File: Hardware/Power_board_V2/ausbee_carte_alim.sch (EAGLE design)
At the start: 22 parts, among them K1 G5LE

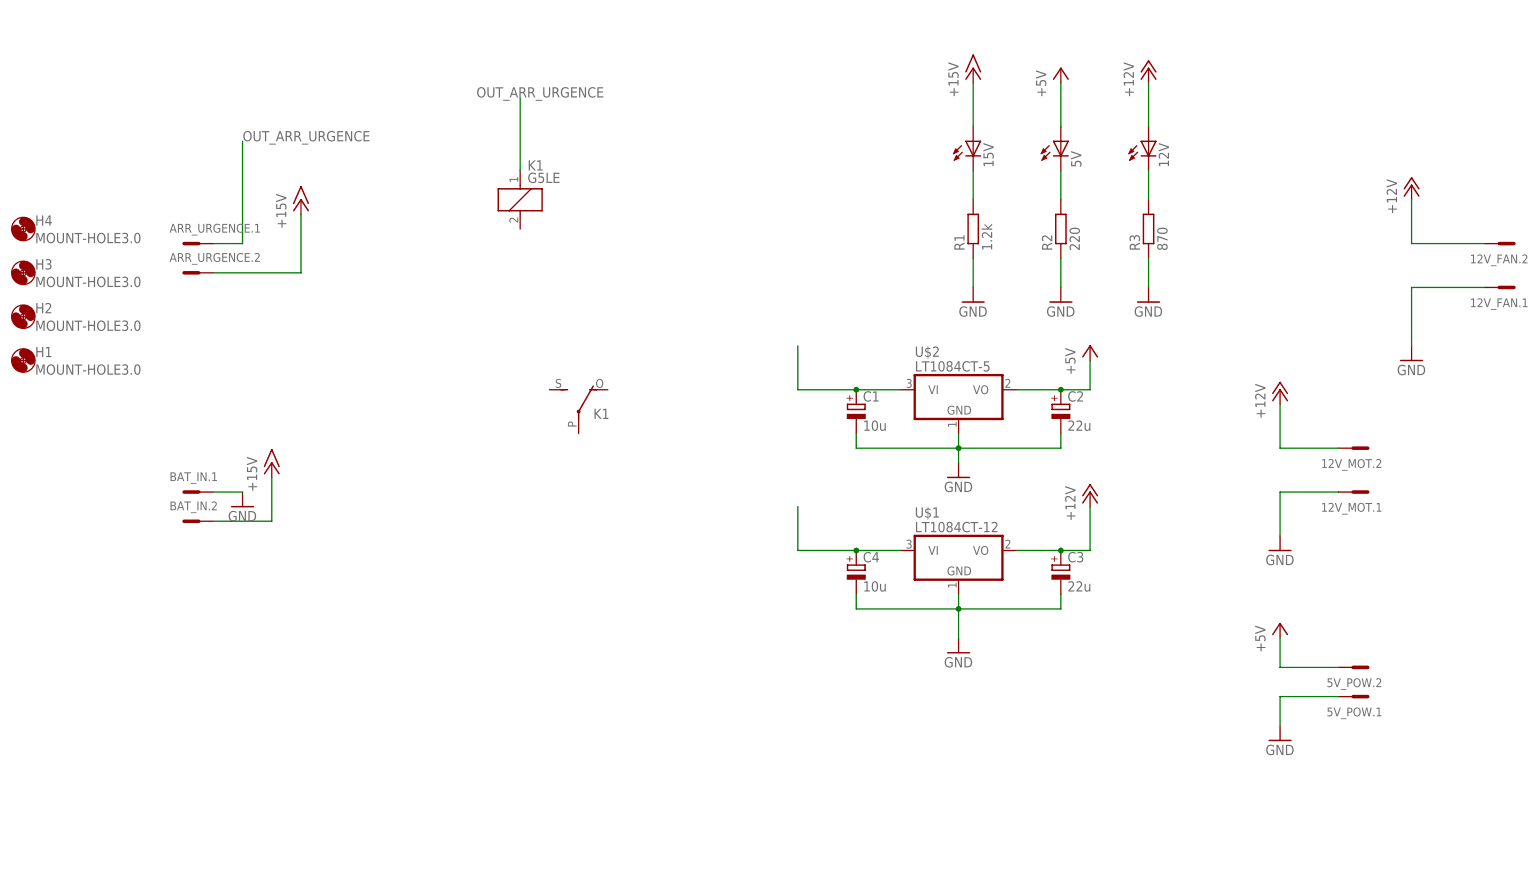
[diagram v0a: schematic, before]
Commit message: Power board V2, adaptator GPIO
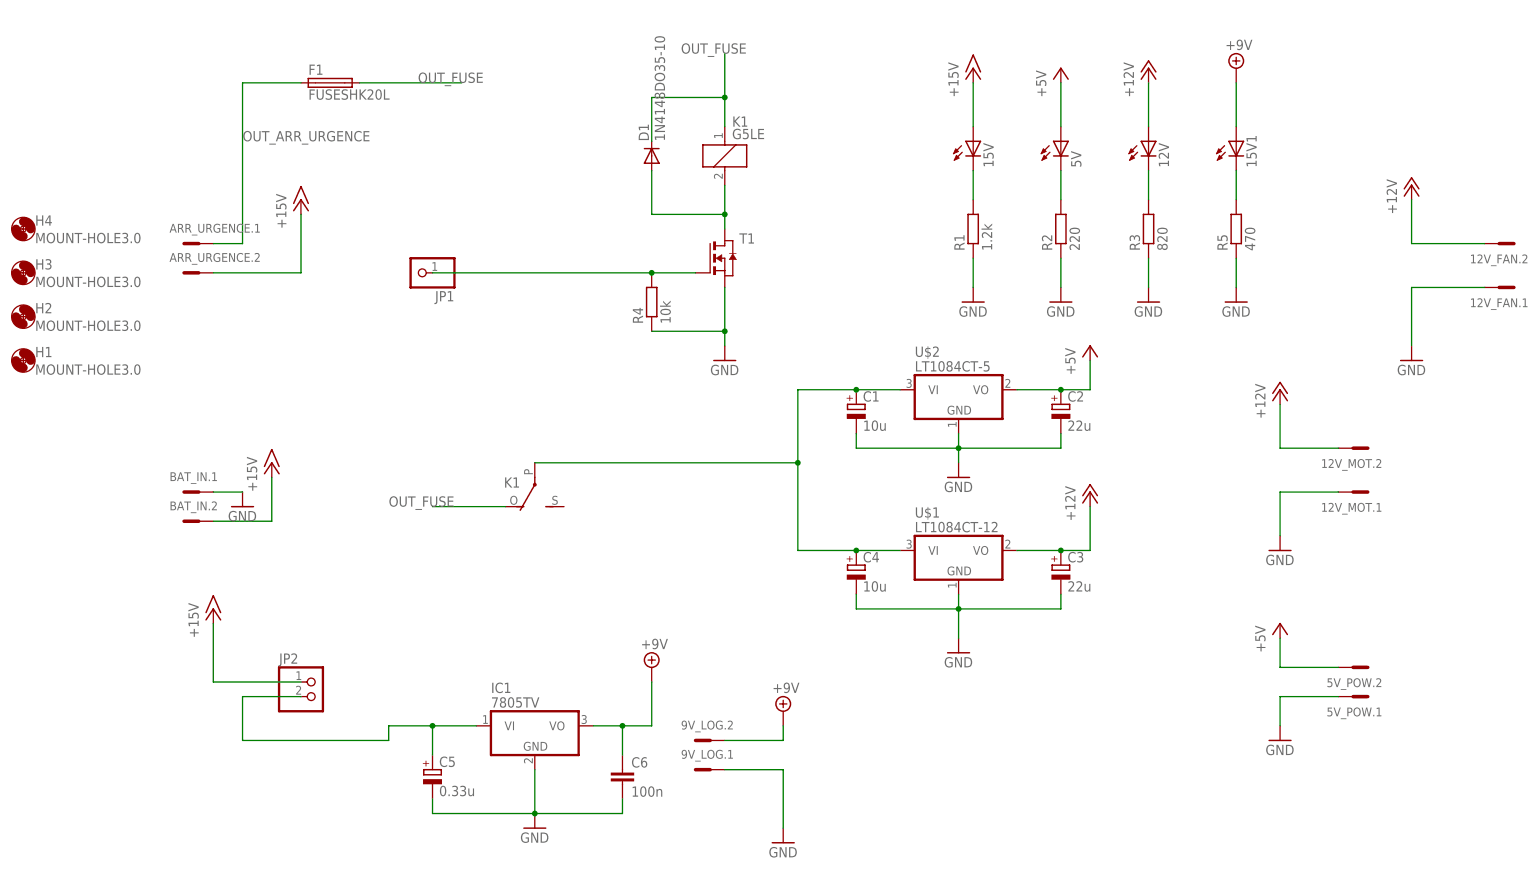
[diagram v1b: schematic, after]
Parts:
- added 15V1: (no value), led:LED3MM
- added 9V_LOG: MCV2, con-phoenix-381_l:MCV2
- added C5: 0.33u, rcl:CPOL-EUE2.5-5
- added C6: 100n, rcl:C-EUC0805
- added D1: 1N4148DO35-10, diode:1N4148DO35-10
- added F1: FUSESHK20L, fuse:FUSESHK20L
- added IC1: 7805TV, linear:7805TV
- added JP1: (no value), pinhead:PINHD-1X1
- added JP2: (no value), pinhead:PINHD-1X2
- added R4: 10k, rcl:R-EU_0309/V
- added R5: 470, rcl:R-EU_0309/V
- added T1: (no value), zetex:NMOSSOT23
- C2, C3: device rcl:CPOL-EUE5-8.5 -> rcl:CPOL-EUCT7343
- R3: value 870 -> 820
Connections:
- new net +9V: 15V1.A, 9V_LOG.2.SK, C6.1, IC1.VO
- new net N$10: 15V1.C, R5.2
- new net N$6: JP1.1, R4.2, T1.G
- new net N$9: C5.+, IC1.VI, JP2.2
- new net OUT_FUSE: D1.C, F1.2, K11.1, K12.O
- net +15V: now also JP2.1
- net GND: now also 9V_LOG.1.SK, C5.-, C6.2, IC1.GND, R4.1, R5.1, T1.S
- net N$4: now also C1.+, K12.P, U$2.VI
- net N$5: now also D1.A, K11.2, T1.D; no longer C1.+, U$2.VI
- net OUT_ARR_URGENCE: now also F1.1; no longer K11.1
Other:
- moved on the sheet: K1
